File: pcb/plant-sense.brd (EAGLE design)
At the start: 48.5 x 48.5 mm, 89 parts, among them CON1 3P-SH-TOP, CON2 3P-SH-TOP, CON3 3P-SH-TOP, CON4 3P-SH-TOP, CON5 4P-SH-TOP, CON6 4P-SH-TOP, CON7 4P-SH-TOP, CON8 4P-SH-TOP, CON9 2P-PH-TOP, Q1 AO3401, T1 BC817, U1 MCP1253-33X50, U15 TP4056, U2 MIC23155, U3 FS312F-G, U4 FS8205, U5 EFM32GG11B520F2048GQ64, U6 SST26VF016B, U7 RFM69HW, U8 SI7021, U9 LTC4316, X1 8MHz

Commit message: pcb work
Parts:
- removed D1: SMAJ5.0A, TVS:DO214AC
- removed D2: B0530W, Generic Diode:SOD-123
- removed F1: 1A Hold, PTC Fuses:1206
- removed Q1: AO3401, Alpha Omega:SOT23
- removed R1, R3: 5.1K Ohms, Resistor:RES0603
- removed R60, R61, R9: 100K Ohms, Resistor:RES0603
- removed R62: 1.5K Ohms, Resistor:RES0603
- removed U15: TP4056, TP4056:SOP-8
- removed USB1: USB-C-16P-SMD-FLAT-SIDE, USB Connector:USB-C-16P-SMD-FLAT-SIDE
- C2: value 100uF -> 100nF; device Capacitor:CAP1206 -> Capacitor:CAP0603
- C4, C5: value 10uF -> 100nF
- U5: value EFM32GG11B520F2048GQ64 -> EFM32PG1B200F256GM32; device EFM32:QFP64 -> EFM32:QFN32
- X1: value 8MHz -> 40MHz; device Crystal:2-SMD-5032 -> Crystal:4-SMD-3225
- moved C23 143.0 mm to (41.0, 7.50)
- moved C25 134.6 mm to (34.0, 30.0)
- moved C7 127.6 mm to (34.0, 18.5), turned to 180 degrees
- moved C24 126.9 mm to (34.0, 37.5)
- moved R26 122.6 mm to (37.5, 7.50)
- moved R25 117.1 mm to (37.5, 5.50)
- moved C22 116.4 mm to (34.9, 41.7), turned to 90 degrees
- moved C21 113.8 mm to (39.2, 46.8), turned to 180 degrees
- moved C5 111.6 mm to (34.0, 33.5), turned to 180 degrees
- moved C4 110.5 mm to (34.0, 26.0), turned to 180 degrees
- moved C8 107.0 mm to (16.3, 38.3), turned to 90 degrees
- moved C19 105.3 mm to (39.2, 45.0), turned to 180 degrees
- moved R13 104.7 mm to (7.50, 7.00), turned to 90 degrees
- moved R22 104.4 mm to (34.0, 13.0), turned to 180 degrees
- moved C6 103.9 mm to (16.0, 26.4), turned to 180 degrees
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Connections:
- removed net !BAT_CHRG: R60.1, U15.7, U5.10
- removed net !BAT_STDBY: R61.1, U15.6, U5.11
- removed net 2V8_PGOOD: R9.1, U2.5, U5.16
- removed net 5V0: C2.1, D1.C, D2.A, F1.1, Q1.1, U15.4, U15.8
- removed net N$21: U5.38
- removed net N$3: R1.2, USB1.CC2
- removed net N$4: F1.2, USB1.VBUS@0, USB1.VBUS@1
- removed net N$46: R62.2, U15.2
- removed net N$5: R3.2, USB1.CC1
- removed net VIN: C4.1, C5.1, C7.1, D2.C, Q1.2, U2.2, U2.8, U2.9
- net !FLASH_CS: now also U5.14; no longer U5.63
- net !RFM_CS: now also U5.13; no longer U5.62
- net !RST: now also U5.8; no longer U5.20
- net 1V8: now also U5.28; no longer U5.41
- net 2V8: now also U5.22, U5.30, U5.5; no longer R60.2, R61.2, R9.2, U5.24, U5.40, U5.55, U5.7
- net GND: now also U5.25, U5.33, X1.2, X1.4; no longer D1.A, R1.1, R3.1, R62.1, U15.1, U15.3, U15.9, U5.23, U5.56, U5.8, USB1.GND@0, USB1.GND@1, USB1.SHIELD@0, USB1.SHIELD@1, USB1.SHIELD@2, USB1.SHIELD@3
- net HSENS1: now also U5.19; no longer U5.30
- net HSENS2: now also U5.20; no longer U5.31
- net HSENS3: now also U5.21; no longer U5.32
- net HSENS4: now also U5.23; no longer U5.33
- net I2C0_SCL: now also U5.10; no longer U5.2
- net I2C0_SDA: now also U5.11; no longer U5.1
- net LED: now also U5.4; no longer U5.54
- net N$16: now also U5.6; no longer U5.26
- net N$17: now also U5.7, X1.3; no longer U5.25, X1.2
- net N$19: now also U5.26; no longer U5.39
- net N$20: now also U5.29; no longer U5.42
- net RFM_IRQ: now also U5.15; no longer U5.13
- net RFM_RST: now also U5.16; no longer U5.64
- net SWCLK: now also U5.1; no longer U5.49
- net SWDIO: now also U5.2; no longer U5.50
- net SWO: now also U5.3; no longer U5.51
- net US0_CLK: now also U5.18; no longer U5.61
- net US0_MISO: now also U5.12; no longer U5.60
- net US0_MOSI: now also U5.17; no longer U5.59
- net VBAT: now also U2.2, U2.8, U2.9; no longer Q1.3, U15.5
- net VBAT_SENSE: now also U5.24; no longer U5.34
- net VEXT: now also C2.1, C4.1, C5.1, C7.1
- net VEXT_EN: now also U5.32; no longer U5.12
- net VEXT_PGOOD: now also U5.31; no longer U5.15
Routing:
- net VEXT: track 0.00 -> 82.7 mm, vias 0 -> 6
- net 2V8: track 0.00 -> 20.2 mm
- net !RST: track 0.00 -> 16.5 mm, vias 0 -> 1
- net VBAT: track 0.00 -> 15.9 mm
- net GBAT: track 0.00 -> 15.7 mm, vias 0 -> 2
- net N$48: track 0.00 -> 6.97 mm
- net N$47: track 0.00 -> 6.63 mm
- net N$13: track 0.00 -> 5.95 mm
- net 1V8: track 0.00 -> 5.72 mm
- net N$16: track 0.00 -> 5.68 mm
- net N$50: track 0.00 -> 5.58 mm
- net N$17: track 0.00 -> 5.52 mm
- net I2C0_SDA_EXT: track 0.00 -> 5.37 mm
- net N$1: track 0.00 -> 5.12 mm
- net I2C0_SCL_EXT: track 0.00 -> 4.75 mm
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- added copper zone on layer 1, net GND
- added copper zone on layer 16, net GND

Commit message: PCB Work
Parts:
- removed D3: LED1206, LED:1206
- removed R24: 330 Ohms, Resistor:RES0603
- removed R25, R26: 10K Ohms, Resistor:RES0603
- added D1: LED1206, LED:1206
- added R1, R3: 100K Ohms, Resistor:RES0603
- added R9: 10M Ohm, Resistor:RES0603
- C1: value 100nF -> 10uF
- C19: value 10uF -> 100nF
- C22: value 1uF -> 470pF
- C23: value 10uF -> 470pF
- C24, C25: value 470pF -> 100nF
- C3: value 100uF -> 100nF; device Capacitor:CAP1206 -> Capacitor:CAP0603
- C4: value 100nF -> 100uF; device Capacitor:CAP0603 -> Capacitor:CAP1206
- C5: value 100nF -> 1uF
- C6: value 470pF -> 10uF
- C7: value 100nF -> 470pF
- CON1: value 3P-SH-TOP -> 2P-PH-TOP; device JST:SH-03-TOP -> JST:PH-02-TOP
- CON5: value 4P-SH-TOP -> 3P-SH-TOP; device JST:SH-04-TOP -> JST:SH-03-TOP
- CON9: value 2P-PH-TOP -> 4P-SH-TOP; device JST:PH-02-TOP -> JST:SH-04-TOP
- R10: value 324K Ohms -> 100K Ohms
- R11: value 91K Ohms -> 100K Ohms
- R12: value 10M Ohm -> 10K Ohms
- R13, R23: value 100K Ohms -> 10K Ohms
- R14: value 10K Ohms -> 330 Ohms
- R15: value 10K Ohms -> 100K Ohms
- R18: value 100K Ohms -> 0 Ohms
- R22: value 0 Ohms -> 10K Ohms
- R5: value 100K Ohms -> 1K Ohms
- R6: value 100K Ohms -> 100 Ohms
- R7: value 1K Ohms -> 324K Ohms
- R8: value 100 Ohms -> 91K Ohms
- moved C20 118.7 mm to (34.0, 18.5), turned to 180 degrees
- moved C28 101.4 mm to (24.8, 6.20), turned to 270 degrees
- moved C18 99.0 mm to (26.5, 28.1), turned to 270 degrees
- moved C9 94.6 mm to (26.5, 37.5), turned to 90 degrees
- moved C13 91.2 mm to (18.9, 9.60), turned to 270 degrees
- moved C14 85.3 mm to (11.0, 14.7), turned to 270 degrees
- moved C17 78.3 mm to (18.6, 44.7), turned to 90 degrees
- moved C12 74.3 mm to (16.0, 24.6), turned to 180 degrees
- moved CON9 48.8 mm to (45.5, 13.0), turned to 270 degrees
- moved C21 46.5 mm to (23.6, 3.00), turned to 0 degrees
- moved R15 43.6 mm to (32.0, 45.5)
- moved CON1 36.5 mm to (3.00, 37.0), turned to 90 degrees
- moved C2 36.2 mm to (39.2, 46.8)
- moved C19 34.4 mm to (34.0, 11.0)
- moved R10 34.0 mm to (7.50, 7.00), turned to 90 degrees
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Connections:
- net !FLASH_CS: now also R15.1; no longer R16.1
- net !RFM_CS: now also R17.1; no longer R18.1
- net !RST: now also R10.1; no longer R13.1
- net 2V8: now also C21.1, R12.2, R17.2, R7.2; no longer C20.1, R16.2, R18.2, R24.2
- net GBAT: now also CON1.2, R9.2; no longer CON9.2, R12.2
- net GND: now also C22.2, CON5.3, CON9.4, R1.1, R16.1, R5.1, R8.1, R9.1; no longer C5.2, CON1.3, CON5.4, R11.1, R12.1, R17.1, R6.1, R7.1
- net HSENS1: now also C22.1, R18.2; no longer C24.1, R19.2
- net HSENS2: now also C23.1, R19.2; no longer C25.1, R20.2
- net HSENS3: now also R20.2; no longer R21.2
- net HSENS4: now also R21.2; no longer R22.2
- net I2C0_SCL: now also R13.1; no longer R15.1
- net I2C0_SCL_EXT: now also CON9.2, R23.1; no longer CON5.2, R26.1
- net I2C0_SDA: now also R12.1; no longer R14.1
- net I2C0_SDA_EXT: now also CON9.3, R22.1; no longer CON5.3, R25.1
- net LED: now also R11.2; no longer R23.2
- net N$10: now also CON5.2, R21.1; no longer CON4.2, R22.1
- net N$11: now also R11.1; no longer R23.1
- net N$13: now also R7.1, R8.2; no longer R10.1, R11.2
- net N$15: now also D1.1; no longer D3.1
- net N$18: now also D1.2, R14.1; no longer D3.2, R24.1
- net N$2: now also C5.2; no longer C22.2
- net N$49: now also R6.1; no longer R8.1
- net N$50: now also R5.2; no longer R7.2
- net N$6: now also C5.1; no longer C22.1
- net N$7: now also CON3.2, R19.1; no longer CON2.2, R20.1
- net N$8: now also CON4.2, R20.1; no longer CON3.2, R21.1
- net N$9: now also CON2.2, R18.1; no longer CON1.2, R19.1
- net RFM_RST: now also R16.2; no longer R17.2
- net VBAT: now also C2.1, C4.1, CON1.1, R3.2, R6.2; no longer C19.1, C21.1, CON9.1, R5.2, R8.2
- net VBAT_SENSE: now also C7.1, R3.1, R4.2; no longer C6.1, R5.1, R6.2
- net VEXT: now also C19.1, C20.1, C24.1, C25.1, C6.1, CON9.1, R22.2, R23.2; no longer C2.1, C23.1, C4.1, C5.1, C7.1, CON1.1, R25.2, R26.2
- net VEXT_EN: now also R1.2; no longer R4.2
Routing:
- net 2V8: track 20.2 -> 151.8 mm, vias 0 -> 10
- net VBAT: track 15.9 -> 73.4 mm, vias 0 -> 2
- net I2C0_SDA_EXT: track 5.37 -> 55.3 mm, vias 0 -> 5
- net I2C0_SCL_EXT: track 4.75 -> 50.0 mm, vias 0 -> 5
- net !RST: track 16.5 -> 45.0 mm, vias 1 -> 2
- net I2C0_SDA: track 0.00 -> 28.2 mm, vias 0 -> 3
- net I2C0_SCL: track 0.00 -> 26.7 mm, vias 0 -> 3
- net SWO: track 0.00 -> 21.9 mm, vias 0 -> 2
- net SWDIO: track 0.00 -> 15.2 mm, vias 0 -> 2
- net SWCLK: track 0.00 -> 14.6 mm, vias 0 -> 2
- net VEXT_PGOOD: track 0.00 -> 11.0 mm, vias 0 -> 2
- net !RFM_CS: track 0.00 -> 9.95 mm, vias 0 -> 1
- net VEXT_EN: track 0.00 -> 6.47 mm, vias 0 -> 2
- net !FLASH_CS: track 0.00 -> 4.53 mm
- net RFM_RST: track 0.00 -> 3.44 mm, vias 0 -> 1
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
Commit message: Change DRCs
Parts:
- added LOGO1: JS-5MM, Silkscreen:JS_5MM
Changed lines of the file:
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@@
 <drawing>
 <settings>
-<setting alwaysvectorfont="no"/>
+<setting alwaysvectorfont="yes"/>
 <setting verticaltext="up"/>
 </settings>
@@
 <param name="rvPadInner" value="0.25"/>
 <param name="rvPadBottom" value="0.25"/>
-<param name="rvViaOuter" value="0.25"/>
-<param name="rvViaInner" value="0.25"/>
+<param name="rvViaOuter" value="0.5"/>
+<param name="rvViaInner" value="0.5"/>
 <param name="rvMicroViaOuter" value="0.25"/>
 <param name="rvMicroViaInner" value="0.25"/>
-<param name="rlMinPadTop" value="10mil"/>
+<param name="rlMinPadTop" value="3mil"/>
 <param name="rlMaxPadTop" value="20mil"/>
-<param name="rlMinPadInner" value="10mil"/>
+<param name="rlMinPadInner" value="3mil"/>
 <param name="rlMaxPadInner" value="20mil"/>
-<param name="rlMinPadBottom" value="10mil"/>
+<param name="rlMinPadBottom" value="3mil"/>
 <param name="rlMaxPadBottom" value="20mil"/>
-<param name="rlMinViaOuter" value="8mil"/>
+<param name="rlMinViaOuter" value="3mil"/>
 <param name="rlMaxViaOuter" value="20mil"/>
-<param name="rlMinViaInner" value="8mil"/>
+<param name="rlMinViaInner" value="3mil"/>
 <param name="rlMaxViaInner" value="20mil"/>
-<param name="rlMinMicroViaOuter" value="4mil"/>
+<param name="rlMinMicroViaOuter" value="3mil"/>
 <param name="rlMaxMicroViaOuter" value="20mil"/>
-<param name="rlMinMicroViaInner" value="4mil"/>
+<param name="rlMinMicroViaInner" value="3mil"/>
 <param name="rlMaxMicroViaInner" value="20mil"/>
 <param name="psTop" value="-1"/>
@@
 <attribute name="VALUE" x="36.9464" y="20.532" size="0.762" layer="27" font="vector" ratio="10" rot="SR180"/>
 </element>
+<element name="LOGO1" library="Silkscreen" package="JS_5MM" value="JS-5MM" x="29.6" y="23" smashed="yes"/>
 </elements>
 <signals>

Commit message: Finish board (needs revision)
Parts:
- U5: device EFM32:QFN32 -> EFM32:QFN32_0.5P
- U7: device HopeRF:RFM69W-XXXS2 -> HopeRF:RFM69XW-XXXS2
- moved X1 0.32 mm to (22.9, 11.2), turned to 180 degrees
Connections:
- net !FLASH_CS: now also U5.13; no longer U5.14
- net !RFM_CS: now also U5.14; no longer U5.13
- net GND: now also X1.1, X1.3; no longer X1.2, X1.4
- net N$16: now also X1.2; no longer X1.1
- net N$17: now also X1.4; no longer X1.3
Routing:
- net VEXT_EN: track 6.47 -> 69.1 mm, vias 2 -> 5
- net US0_MISO: track 0.00 -> 57.6 mm, vias 0 -> 2
- net US0_CLK: track 0.00 -> 51.7 mm, vias 0 -> 2
- net VEXT_PGOOD: track 11.0 -> 61.3 mm, vias 2 -> 3
- net US0_MOSI: track 0.00 -> 46.6 mm, vias 0 -> 2
- net RFM_RST: track 3.44 -> 42.5 mm, vias 1 -> 4
- net RFM_IRQ: track 0.00 -> 38.4 mm, vias 0 -> 5
- net !FLASH_CS: track 4.53 -> 34.2 mm, vias 0 -> 2
- net LED: track 0.00 -> 27.0 mm, vias 0 -> 2
- net HSENS1: track 2.00 -> 26.5 mm, vias 0 -> 2
- net !RFM_CS: track 9.95 -> 34.3 mm, vias 1 -> 2
- net HSENS4: track 2.00 -> 21.2 mm, vias 0 -> 2
- net HSENS2: track 2.00 -> 21.0 mm, vias 0 -> 2
- net I2C0_SDA: track 28.2 -> 46.9 mm, vias 3 -> 4
- net HSENS3: track 2.00 -> 19.6 mm, vias 0 -> 2
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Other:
- board text added: "IoT Plant sense v1 Jul 2019"

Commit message: Finish machine gun
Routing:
- net GND: vias 10 -> 398

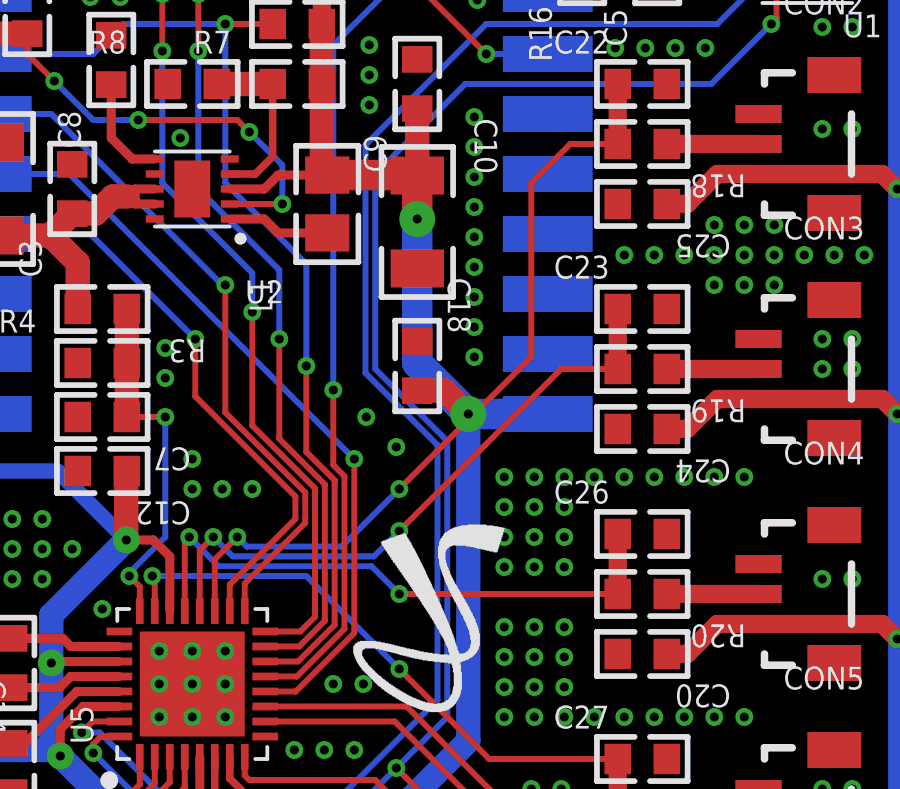
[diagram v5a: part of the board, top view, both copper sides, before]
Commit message: Changed DRC Fixed overlapping traces
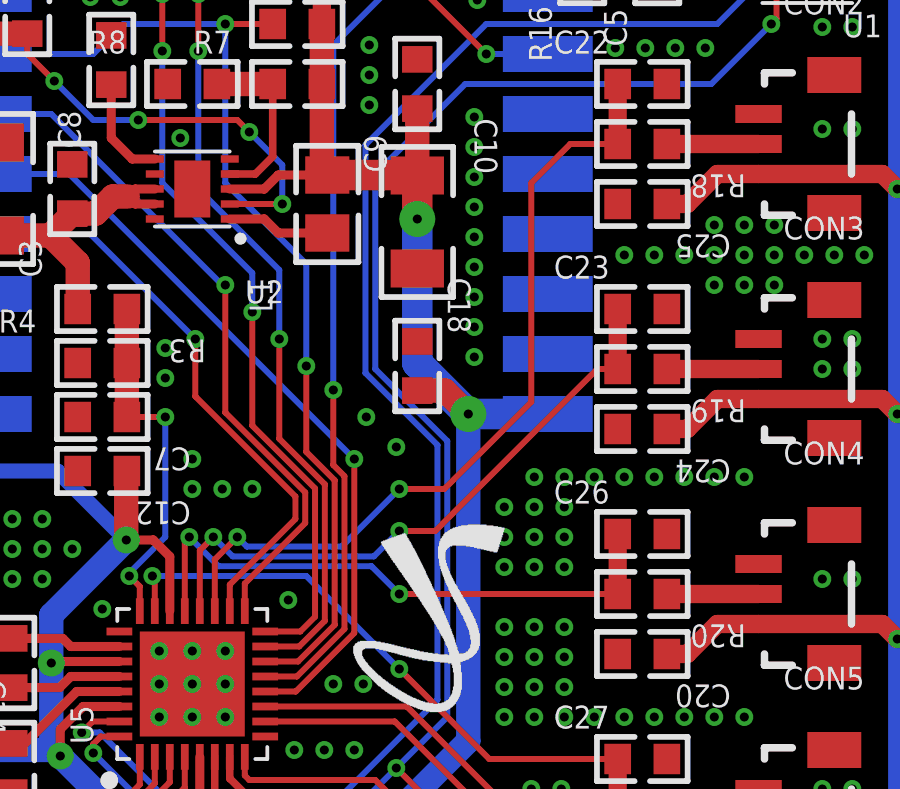
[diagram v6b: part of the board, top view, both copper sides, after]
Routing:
- net HSENS1: track 26.5 -> 27.4 mm
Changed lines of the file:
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@@
 <?xml version="1.0" encoding="utf-8"?>
 <!DOCTYPE eagle SYSTEM "eagle.dtd">
-<eagle version="9.4.2">
+<eagle version="9.5.1">
 <drawing>
 <settings>
@@
 </class>
 </classes>
-<designrules name="jlcpcb">
+<designrules name="jlcpcb_2layer">
 <description language="de">&lt;b&gt;EAGLE Design Rules&lt;/b&gt;
 &lt;p&gt;
@@
 <param name="mvStopFrame" value="1"/>
 <param name="mvCreamFrame" value="0"/>
-<param name="mlMinStopFrame" value="4mil"/>
-<param name="mlMaxStopFrame" value="4mil"/>
+<param name="mlMinStopFrame" value="0.075mm"/>
+<param name="mlMaxStopFrame" value="0.075mm"/>
 <param name="mlMinCreamFrame" value="0mil"/>
 <param name="mlMaxCreamFrame" value="0mil"/>
@@
 <via x="30.4" y="23.4" extent="1-16" drill="0.3"/>
 <via x="31.4" y="23.4" extent="1-16" drill="0.3"/>
-<via x="29.4" y="24.4" extent="1-16" drill="0.3"/>
 <via x="30.4" y="24.4" extent="1-16" drill="0.3"/>
 <via x="31.4" y="24.4" extent="1-16" drill="0.3"/>
@@
 <via x="33" y="4" extent="1-16" drill="0.3"/>
 <via x="32" y="4" extent="1-16" drill="0.3"/>
-<wire x1="33" y1="4" x2="34" y2="4" width="0" layer="19" extent="1-1"/>
-<wire x1="32" y1="4" x2="33" y2="4" width="0" layer="19" extent="1-1"/>
-<wire x1="34" y1="5" x2="34" y2="4" width="0" layer="19" extent="1-1"/>
+<via x="22.2" y="20.3" extent="1-16" drill="0.3"/>
 </signal>
 <signal name="N$47">
@@
 <via x="25.9" y="24" extent="1-16" drill="0.3"/>
 <wire x1="20.819" y1="22.081" x2="23.981" y2="22.081" width="0.2" layer="16"/>
-<wire x1="25.9" y1="24" x2="30.3" y2="28.4" width="0.2" layer="1"/>
+<wire x1="25.9" y1="24" x2="27.4" y2="24" width="0.2" layer="1"/>
+<wire x1="30.3" y1="26.9" x2="27.4" y2="24" width="0.2" layer="1"/>
 <wire x1="31.6" y1="35.5" x2="33.18085" y2="35.5" width="0.2" layer="1"/>
-<wire x1="30.3" y1="28.4" x2="30.3" y2="34.2" width="0.2" layer="1"/>
+<wire x1="30.3" y1="26.9" x2="30.3" y2="34.2" width="0.2" layer="1"/>
 <wire x1="30.3" y1="34.2" x2="31.6" y2="35.5" width="0.2" layer="1"/>
 </signal>
@@
 <wire x1="25.054" y1="21.754" x2="25.9" y2="22.6" width="0.2" layer="16"/>
 <via x="25.9" y="22.6" extent="1-16" drill="0.3"/>
-<wire x1="25.9" y1="22.6" x2="31.3" y2="28" width="0.2" layer="1"/>
-<wire x1="31.3" y1="28" x2="33.18085" y2="28" width="0.2" layer="1"/>
+<wire x1="25.9" y1="22.6" x2="27.1" y2="22.6" width="0.2" layer="1"/>
+<wire x1="32.5" y1="28" x2="27.1" y2="22.6" width="0.2" layer="1"/>
+<wire x1="32.5" y1="28" x2="33.18085" y2="28" width="0.2" layer="1"/>
 <wire x1="20.346" y1="21.754" x2="25.054" y2="21.754" width="0.2" layer="16"/>
 </signal>
@@
 <mfgpreviewcolor name="substratecolor" color="0xFF786E46"/>
 </mfgpreviewcolors>
+<errors>
+</errors>
 </board>
 </drawing>
